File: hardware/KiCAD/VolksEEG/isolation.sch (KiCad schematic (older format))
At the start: 28 parts

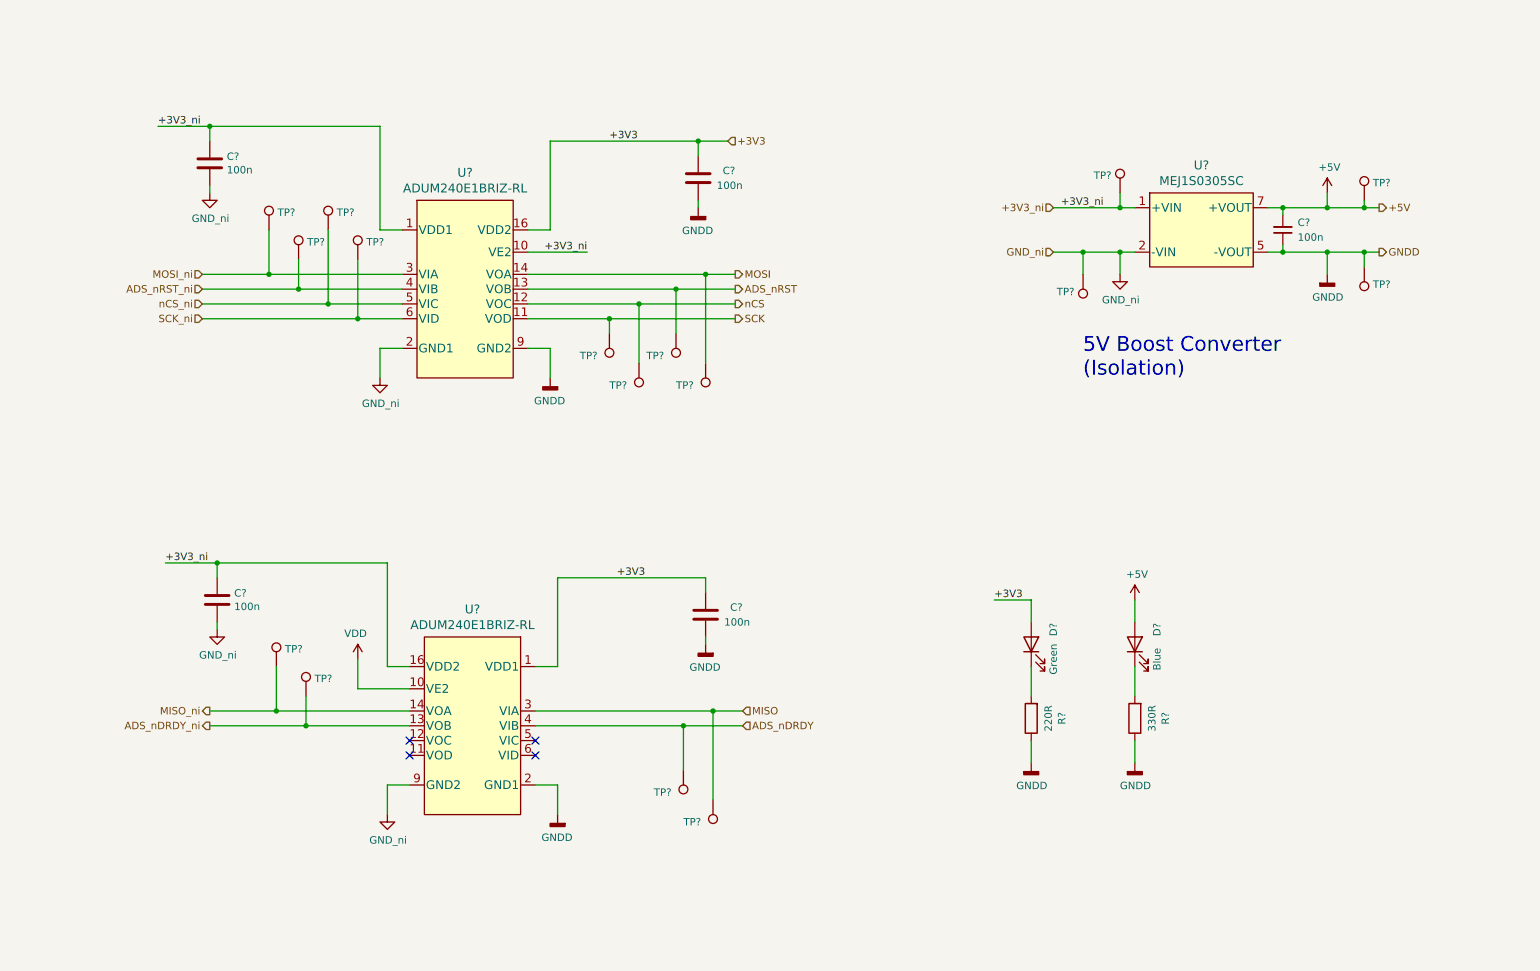
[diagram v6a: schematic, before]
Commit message: Annotated schematic and cleared ERC errors.
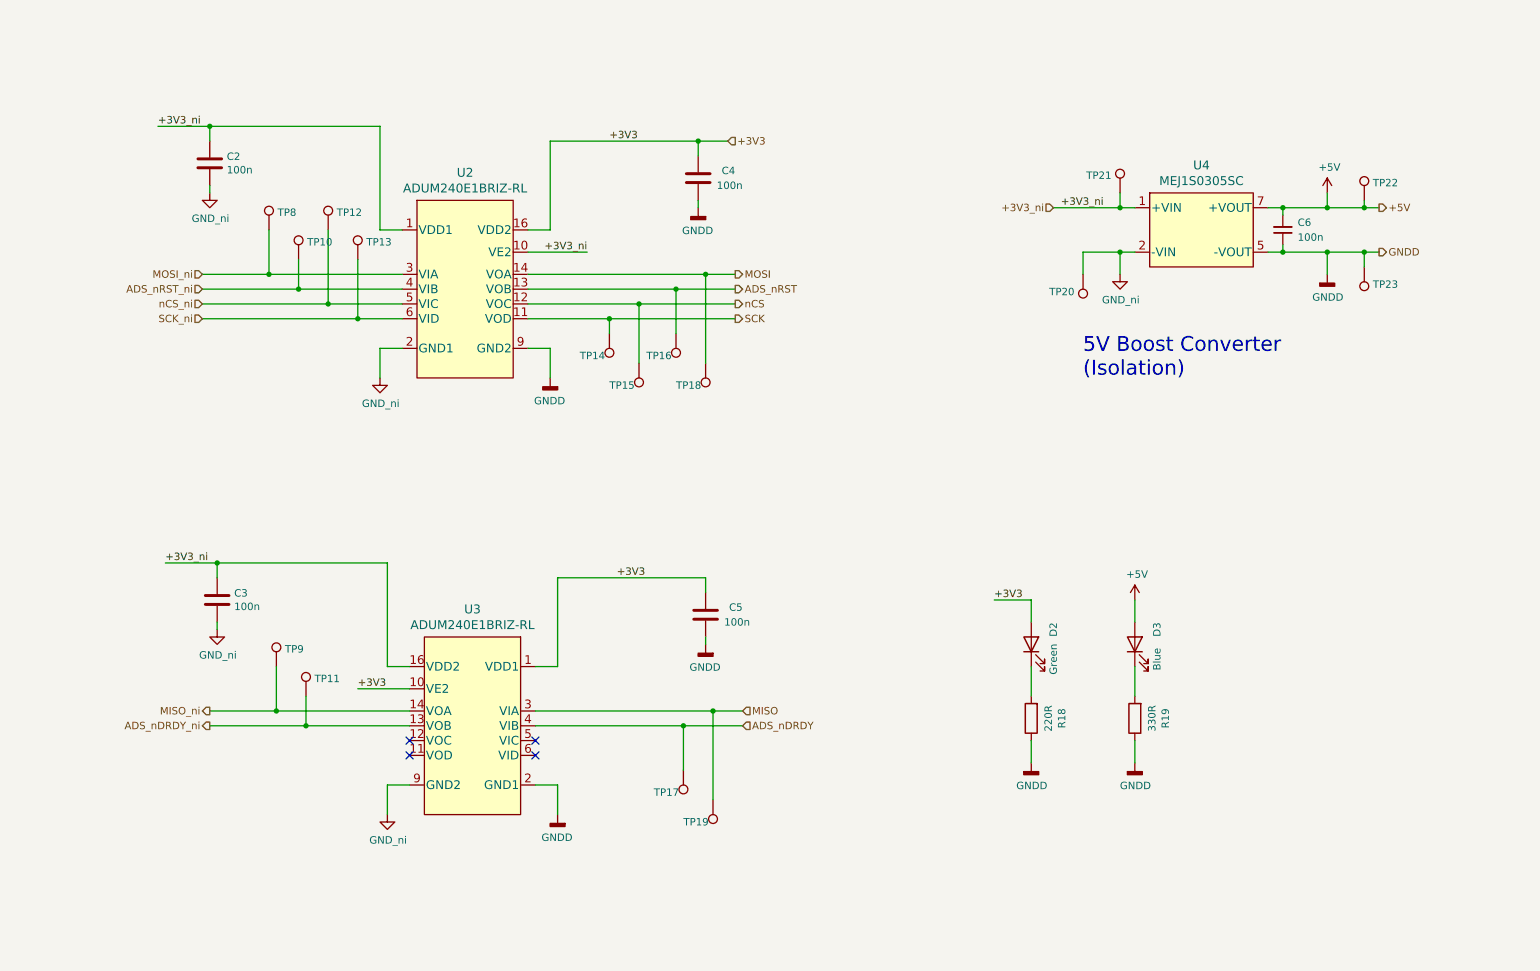
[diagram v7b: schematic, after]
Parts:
- gave numbers to parts that had none: 28
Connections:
- net VDD is gone; now on net +3V3: U3.10 (VE2)

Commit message: General schematic cleanup, and assigning some footprints.
Cleaning up the meta-data within KiCAD, and assigning some basic footprints.
Also, cleaning out some footprint references that didn't point anywhere.
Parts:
- added JP? (x2): Jumper_NC_Small, symbol Device:Jumper_NC_Small
- C2, C3, C4, C5: footprint (none) -> Capacitor_SMD:C_0603_1608Metric_Pad1.08x0.95mm_HandSolder; symbol Device:C -> Device:C_Small
- C6: footprint (none) -> Capacitor_SMD:C_0603_1608Metric_Pad1.08x0.95mm_HandSolder
- R18, R19: footprint (none) -> Resistor_SMD:R_0603_1608Metric_Pad0.98x0.95mm_HandSolder
- TP10, TP11: value ADS_nRST_ni_tp -> TestPoint
- TP12: value nCS_ni_tp -> TestPoint
- TP13: value SCK_ni_tp -> TestPoint
- TP14: value SCK_tp -> TestPoint
- TP15: value nCS_tp -> TestPoint
- TP16, TP17: value ADS_nRST_tp -> TestPoint
- TP18, TP19: value MOSI_tp -> TestPoint
- TP20, TP21, TP23: value GNDD_tp -> TestPoint
- TP22: value 5V_tp -> TestPoint
- TP8, TP9: value MOSI_ni_tp -> TestPoint
- U2, U3: footprint RI_16_2_ADI -> (none)
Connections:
- net +3V3: now also JP?.1; no longer U3.10 (VE2)
- net +3V3_ni: now also JP?.2; no longer U2.10 (VE2)
- new net: JP?.1, U2.10 (VE2)
- new net: JP?.2, U3.10 (VE2)
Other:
- moved on the sheet: C2, C3, C4, C5, TP10, TP11, TP12, TP13, TP17, TP19, TP8, TP9
